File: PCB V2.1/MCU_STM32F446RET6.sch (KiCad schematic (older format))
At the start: 0 parts

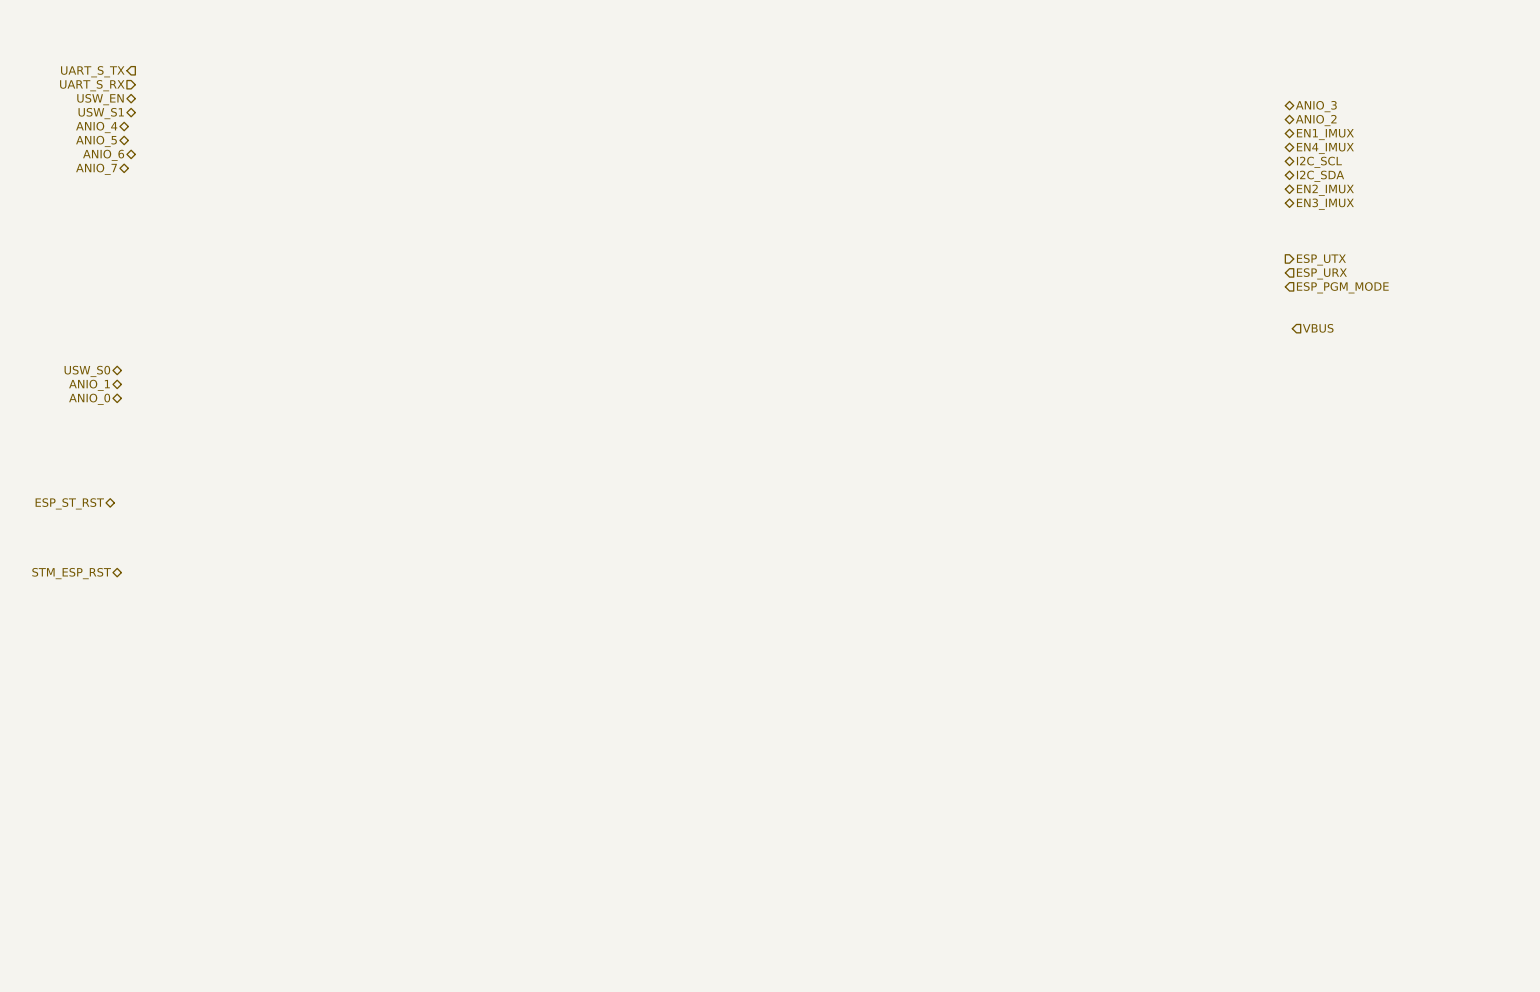
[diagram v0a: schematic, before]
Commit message: SunLeaf Alpha 0.2 and KiCAD Port
SunLeaf rev 2 called Alhpa 0.2 or 0.2a is the main component of this
commit. The entire hardware project has been ported to KiCAD libaries
and all. 0.2a features a revised formfactor, better ESP module, and many
fixes over the original. This version will also be capable of OTA
updates.
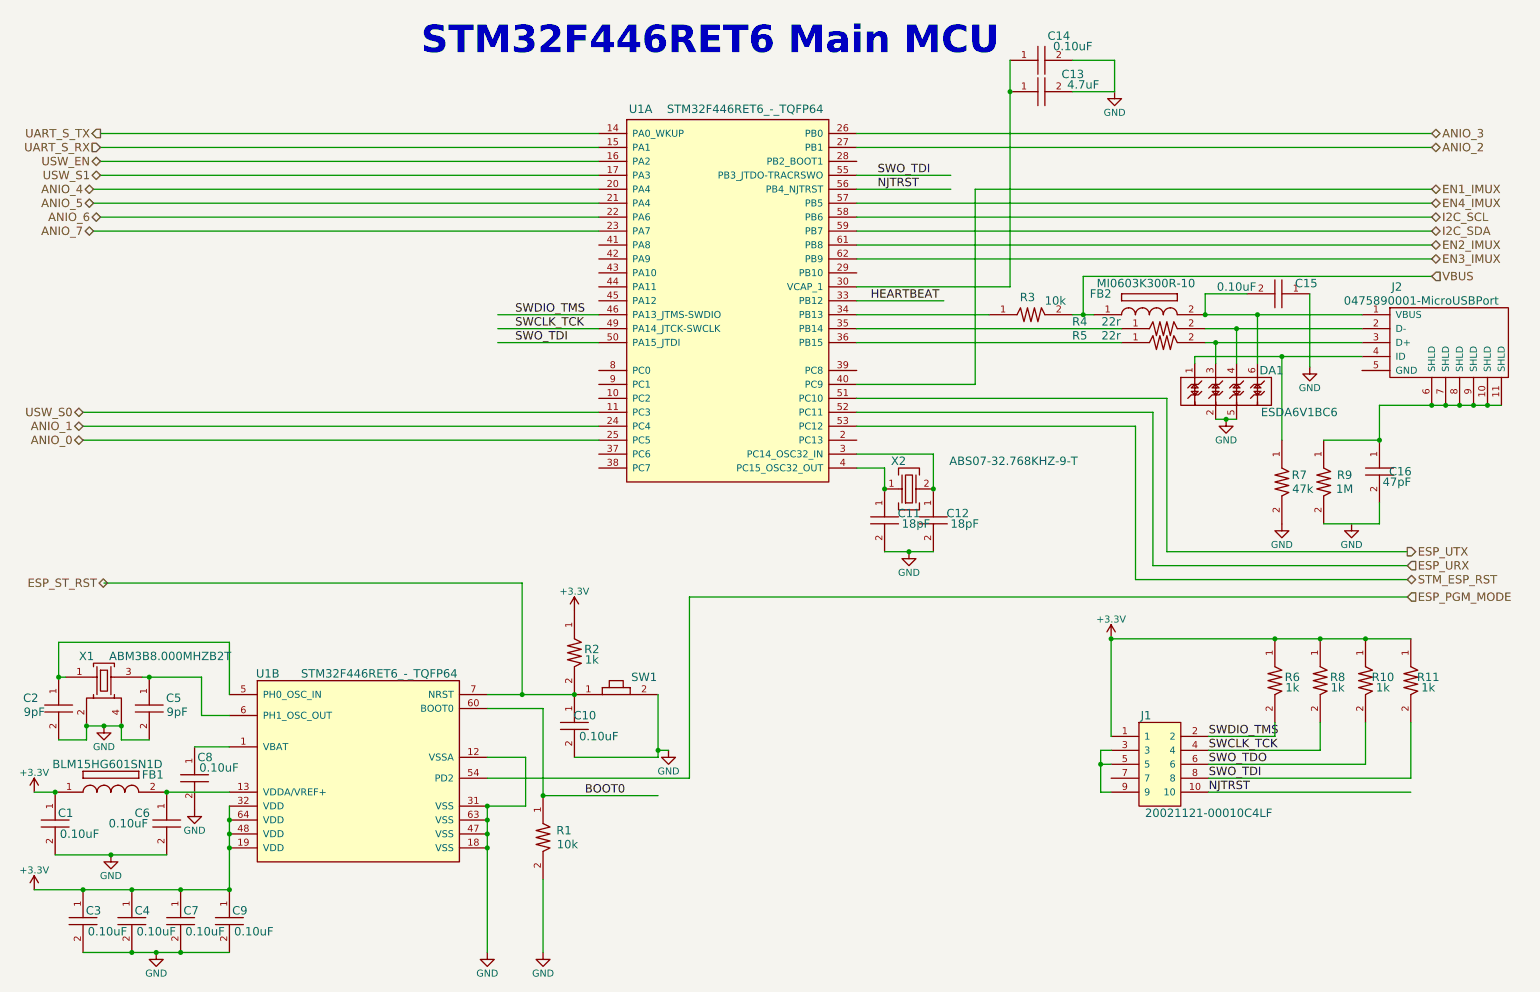
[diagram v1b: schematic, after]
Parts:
- added C1, C10, C14, C15, C3, C4, C6, C7, C8, C9: CL05B104JP5NNNC, PCB_Footprints:C0402, symbol CL05B104JP5NNNC
- added C11, C12: CL05C180GB5NCNC, PCB_Footprints:C0402, symbol CL05C180GB5NCNC
- added C13: CL05A475KQ5NRNC, PCB_Footprints:C0402, symbol CL05A475KQ5NRNC
- added C16: CL05C470FB5NNNC, PCB_Footprints:C0402, symbol CL05C470FB5NNNC
- added C2, C5: CL05C090CB5NNNC, PCB_Footprints:C0402, symbol CL05C090CB5NNNC
- added DA1: ESDA6V1BC6, PCB_Footprints:ESDA6V1BC6, symbol ESDA6V1BC6
- added FB1: BLM15HG601SN1D, PCB_Footprints:BLM15HG601SN1D, symbol BLM15HG601SN1D
- added FB2: MI0603K300R-10, PCB_Footprints:MI0603K300R-10, symbol MI0603K300R-10
- added J1: 20021121-00010C4LF, PCB_Footprints:20021121-00010C4LF, symbol 20021121-00010C4LF
- added J2: 0475890001-MicroUSBPort, PCB_Footprints:0475890001, symbol 0475890001-MicroUSBPort
- added R1, R3: RC1005F103CS, PCB_Footprints:R0402, symbol RC1005F103CS
- added R10, R11, R2, R6, R8: RC1005F102CS, PCB_Footprints:R0402, symbol RC1005F102CS
- added R4, R5: CPF0402B22RE1, PCB_Footprints:R0402, symbol CPF0402B22RE1
- added R7: RC1005J473CS, PCB_Footprints:R0402, symbol RC1005J473CS
- added R9: RC1005F105CS, PCB_Footprints:R0402, symbol RC1005F105CS
- added SW1: B3U-1000P, PCB_Footprints:B3U-1000P, symbol B3U-1000P
- added U1: STM32F446RET6_-_TQFP64, PCB_Footprints:STM32F446RET6, symbol STM32F446RET6_-_TQFP64
- added X1: ABM3B8.000MHZB2T, PCB_Footprints:ABM3B8.000MHZB2T, symbol ABM3B8.000MHZB2T
- added X2: ABS07-32.768KHZ-9-T, PCB_Footprints:ABS07-32.768KHZ-9-T, symbol ABS07-32.768KHZ-9-T
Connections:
- net labels added: +3.3V, BOOT0, GND, HEARTBEAT, NJTRST, SWCLK_TCK, SWDIO_TMS, SWO_TDI, SWO_TDO
- wire segments 0 -> 121
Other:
- note added: "STM32F446RET6 Main MCU"

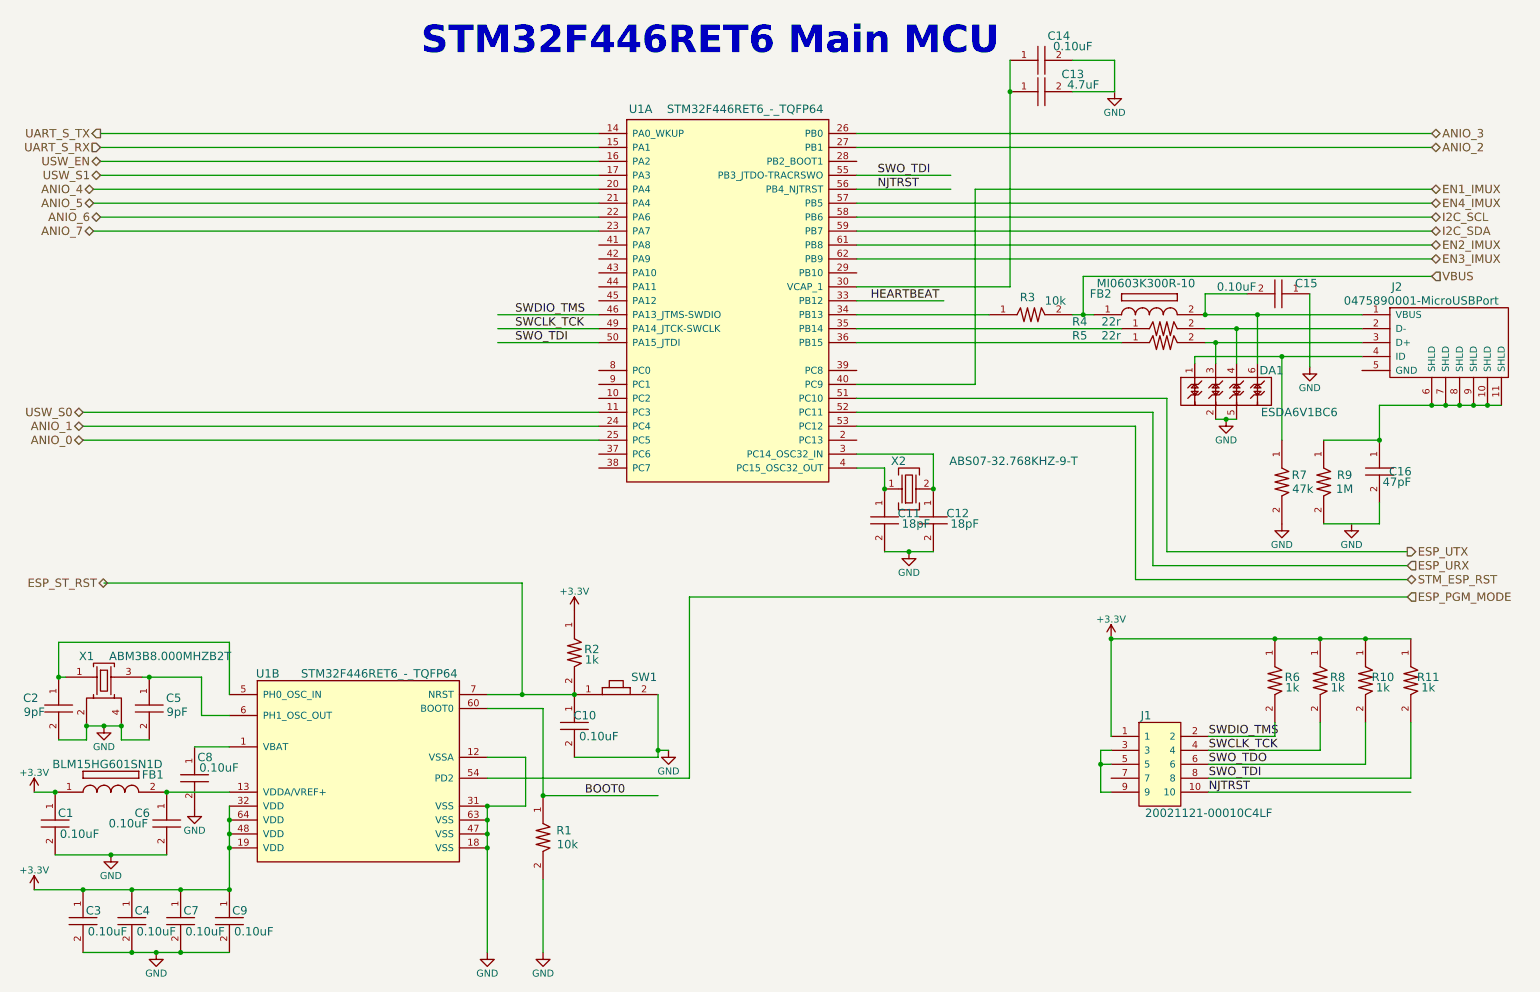
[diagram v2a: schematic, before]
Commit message: Placement
Heavy progress on component placement in KiCAD for SunLEaf V2,
committing to save progress, nightly builds of KiCAD are very crash
prone.
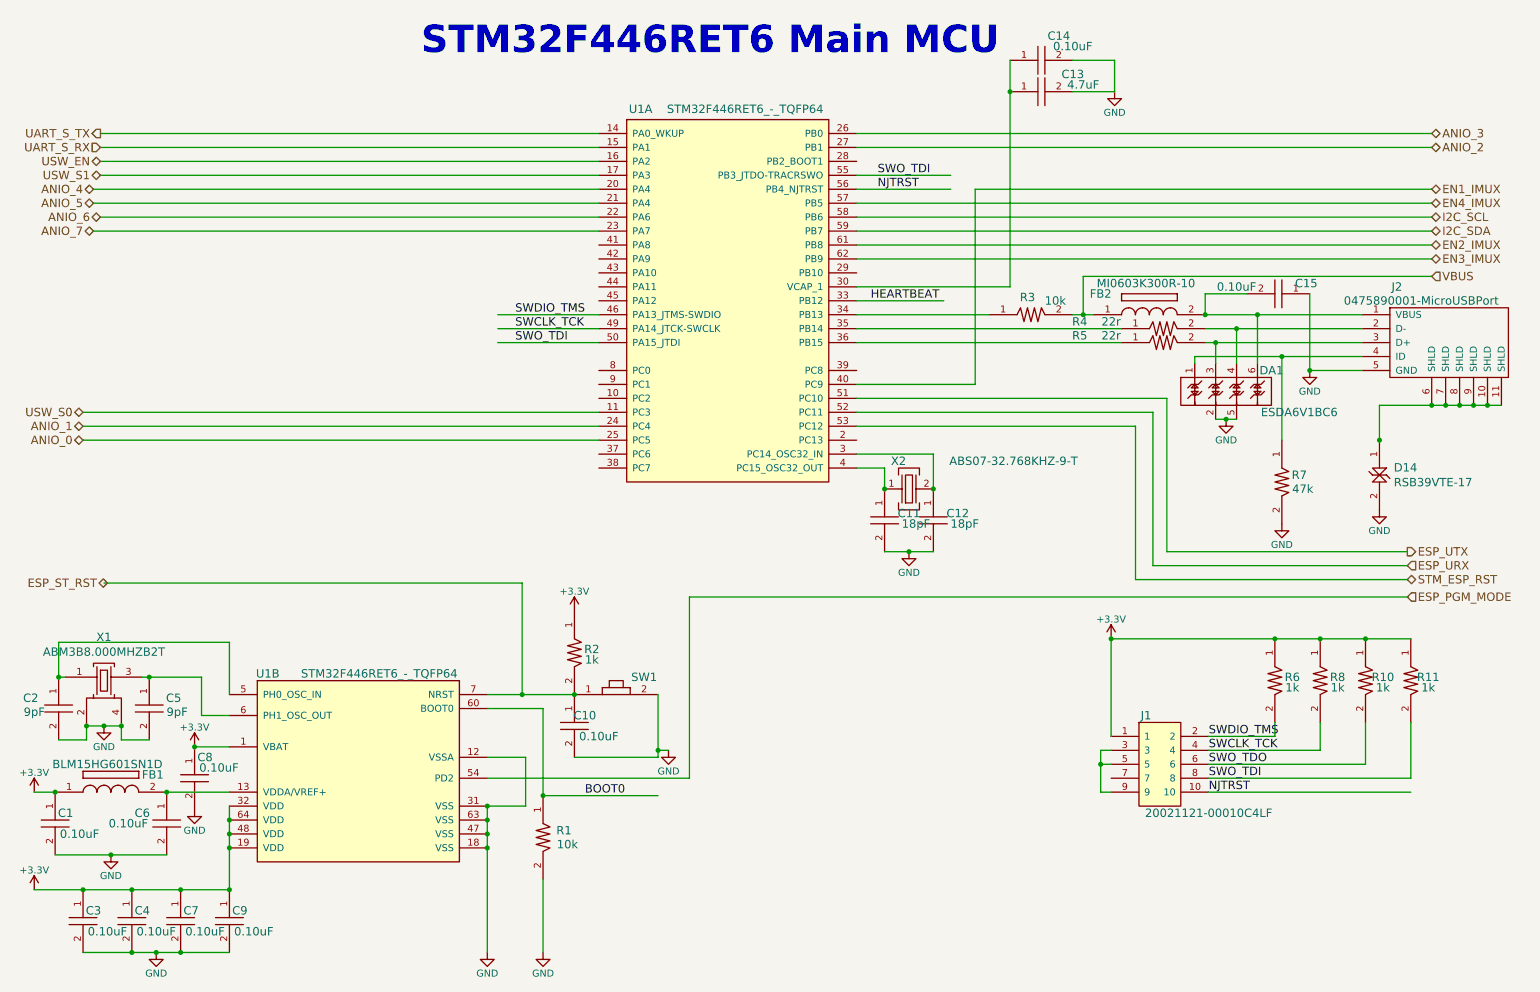
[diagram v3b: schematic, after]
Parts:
- removed C16: CL05C470FB5NNNC, PCB_Footprints:C0402, symbol CL05C470FB5NNNC
- removed R9: RC1005F105CS, PCB_Footprints:R0402, symbol RC1005F105CS
- added D14: RSB39VTE-17, PCB_Footprints:RSB39VTE-17, symbol RSB39VTE-17
- X1: Date Modified 5 Sept 2016 -> 14 Sept 2016
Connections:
- wire segments 121 -> 119

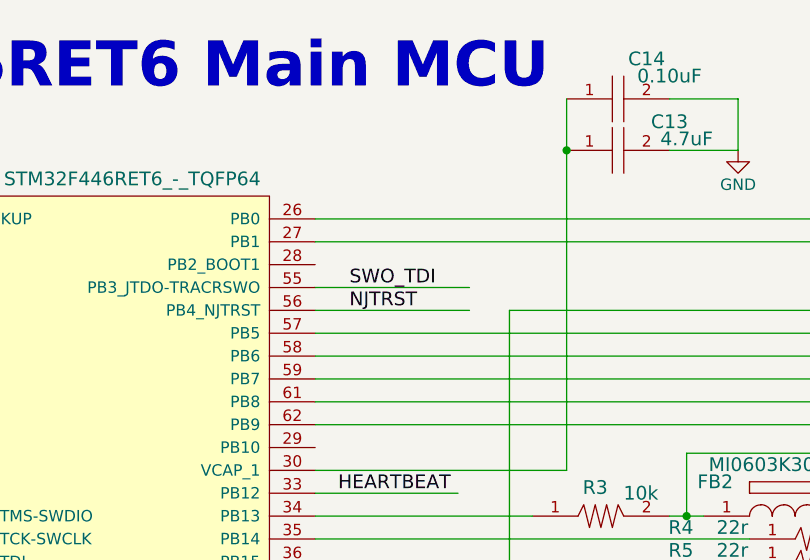
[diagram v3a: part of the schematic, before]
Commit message: Routing and Placement
Placement complete routing has begun. The board size has also been
solidified.
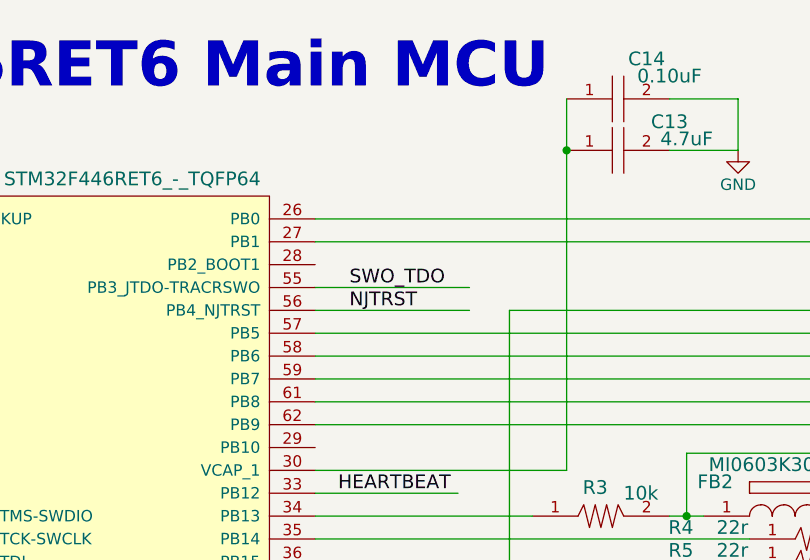
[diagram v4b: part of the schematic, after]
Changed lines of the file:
@@
 NJTRST
 Text Label 6625 1750 0    60   ~ 0
-SWO_TDI
+SWO_TDO
 Wire Wire Line
 	8025 1150 8325 1150

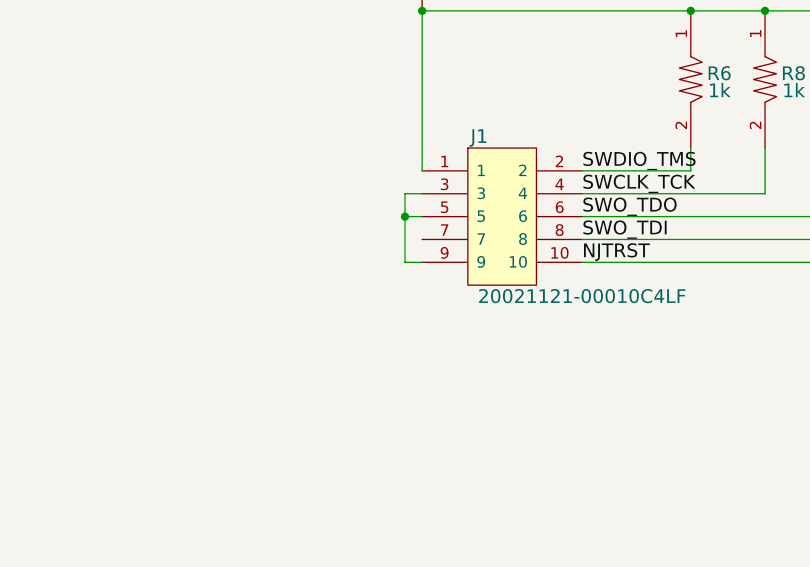
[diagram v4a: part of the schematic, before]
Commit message: Routing Progress
Routing progress made, UART and I2C sensors routed, ESP routed, power
section and solar batter routed, USB routed.
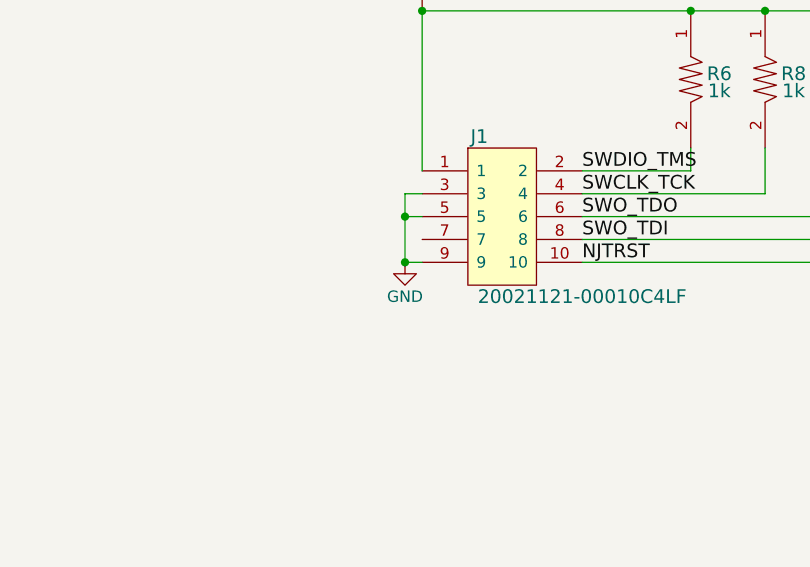
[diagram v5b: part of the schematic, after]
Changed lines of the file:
@@
 	0    1    1    0
 $EndComp
+$Comp
+L GND #PWR?
+U 1 1 57DDB978
+P 8225 6175
+F 0 "#PWR?" H 8225 5925 50  0001 C CNN
+F 1 "GND" H 8225 6025 50  0000 C CNN
+F 2 "" H 8225 6175 50  0000 C CNN
+F 3 "" H 8225 6175 50  0000 C CNN
+	1    8225 6175
+	1    0    0    -1
+$EndComp
+Connection ~ 8225 6175
 $EndSCHEMATC
